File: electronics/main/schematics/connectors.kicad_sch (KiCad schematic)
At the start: 2 parts, among them J1 IN, J2 SW

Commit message: aux voltage
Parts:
- added X1, X3: 345V - Lila, TestPoint:TestPoint_THTPad_D3.0mm_Drill1.5mm, symbol Connector:TestPoint
- added X2: CT_HV - Grau, TestPoint:TestPoint_THTPad_D3.0mm_Drill1.5mm, symbol Connector:TestPoint
- added X4, X6: 3.13V - Grün, TestPoint:TestPoint_THTPad_D3.0mm_Drill1.5mm, symbol Connector:TestPoint
- added X5: CT_HEAT - Schwarz, TestPoint:TestPoint_THTPad_D3.0mm_Drill1.5mm, symbol Connector:TestPoint
- added X7: 12,6V - Rot, TestPoint:TestPoint_THTPad_D3.0mm_Drill1.5mm, symbol Connector:TestPoint
- added X8: 0V - Rot, TestPoint:TestPoint_THTPad_D3.0mm_Drill1.5mm, symbol Connector:TestPoint
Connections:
- new net V_Aux_N: X8.1
- new net V_Aux_P: X7.1
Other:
- note added: "Aux Voltage Input"
- note added: "Foot Switch Input"
- note added: "Guitar Input"
- note added: "HV Input"
- note added: "Heater Power Input"
- moved on the sheet: J1, J2

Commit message: widerstände angelegt
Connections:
- net GND-AUD: now reaches J1.1
- net GND-AUD: now also J1.4, J1.5, J1.6
- net Audio_IN: now reaches J1.2
- net Audio_IN: now also J1.3
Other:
- moved on the sheet: J1
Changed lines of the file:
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@@
+		)
+	)
+	(junction
+		(at 58.42 36.83)
+		(diameter 0)
+		(color 0 0 0 0)
+	)
+	(junction
+		(at 58.42 31.75)
+		(diameter 0)
+		(color 0 0 0 0)
+	)
+	(junction
+		(at 58.42 39.37)
+		(diameter 0)
+		(color 0 0 0 0)
+	)
+	(junction
+		(at 53.34 26.67)
+		(diameter 0)
+		(color 0 0 0 0)
+	)
+	(wire
+		(pts
+			(xy 49.53 29.21) (xy 58.42 29.21)
+		)
+		(stroke
+			(width 0)
+			(type default)
+		)
+	)
+	(wire
+		(pts
+			(xy 53.34 26.67) (xy 58.42 26.67)
+		)
+		(stroke
+			(width 0)
+			(type default)
 		)
 	)
@@
 	(wire
 		(pts
+			(xy 58.42 36.83) (xy 58.42 39.37)
+		)
+		(stroke
+			(width 0)
+			(type default)
+		)
+	)
+	(wire
+		(pts
+			(xy 58.42 29.21) (xy 58.42 31.75)
+		)
+		(stroke
+			(width 0)
+			(type default)
+		)
+	)
+	(wire
+		(pts
+			(xy 49.53 31.75) (xy 58.42 31.75)
+		)
+		(stroke
+			(width 0)
+			(type default)
+		)
+	)
+	(wire
+		(pts
+			(xy 58.42 39.37) (xy 58.42 41.91)
+		)
+		(stroke
+			(width 0)
+			(type default)
+		)
+	)
+	(wire
+		(pts
+			(xy 53.34 34.29) (xy 53.34 26.67)
+		)
+		(stroke
+			(width 0)
+			(type default)
+		)
+	)
+	(wire
+		(pts
+			(xy 49.53 34.29) (xy 53.34 34.29)
+		)
+		(stroke
+			(width 0)
+			(type default)
+		)
+	)
+	(wire
+		(pts
+			(xy 49.53 39.37) (xy 58.42 39.37)
+		)
+		(stroke
+			(width 0)
+			(type default)
+		)
+	)
+	(wire
+		(pts
+			(xy 58.42 31.75) (xy 58.42 36.83)
+		)
+		(stroke
+			(width 0)
+			(type default)
+		)
+	)
+	(wire
+		(pts
+			(xy 49.53 36.83) (xy 58.42 36.83)
+		)
+		(stroke
+			(width 0)
+			(type default)
+		)
+	)
+	(wire
+		(pts
 			(xy 40.64 175.26) (xy 54.61 175.26)
+		)
+		(stroke
+			(width 0)
+			(type default)
+		)
+	)
+	(wire
+		(pts
+			(xy 49.53 26.67) (xy 53.34 26.67)
 		)
 		(stroke
@@
 		)
 	)
+	(hierarchical_label "Audio_IN"
+		(shape output)
+		(at 58.42 26.67 0)
+		(effects
+			(font
+				(size 1.27 1.27)
+			)
+			(justify left)
+		)
+	)
 	(symbol
 		(lib_id "Connector:TestPoint")
@@
 	(symbol
 		(lib_id "wb50_symbols:WB50_Jack_TRS_6pin_Switched")
-		(at 41.91 35.56 0)
+		(at 41.91 33.02 0)
 		(unit 1)
 		(exclude_from_sim no)
@@
 		(fields_autoplaced yes)
 		(property "Reference" "J1"
+			(at 40.64 17.78 0)
+			(effects
+				(font
+					(size 1.27 1.27)
+				)
+			)
+		)
+		(property "Value" "IN"
 			(at 40.64 20.32 0)
 			(effects
@@
 			)
 		)
-		(property "Value" "IN"
+		(property "Footprint" "wb50_footprints:WB50_Jack_TRS_6pin_16.2mm"
 			(at 40.64 22.86 0)
 			(effects
@@
 			)
 		)
-		(property "Footprint" "wb50_footprints:WB50_Jack_TRS_6pin_16.2mm"
-			(at 40.64 25.4 0)
-			(effects
-				(font
-					(size 1.27 1.27)
-				)
-			)
-		)
 		(property "Datasheet" ""
-			(at 41.91 35.56 0)
+			(at 41.91 33.02 0)
 			(effects
 				(font
@@
 		)
 		(property "Description" ""
-			(at 41.91 35.56 0)
+			(at 41.91 33.02 0)
 			(effects
 				(font
@@
 					(unit 1)
 				)
+			)
+		)
+	)
+	(symbol
+		(lib_id "power:GND")
+		(at 58.42 41.91 0)
+		(unit 1)
+		(exclude_from_sim no)
+		(in_bom yes)
+		(on_board yes)
+		(dnp no)
+		(fields_autoplaced yes)
+		(property "Reference" "#PWR07"
+			(at 58.42 48.26 0)
+			(effects
+				(font
+					(size 1.27 1.27)
+				)
+				(hide yes)
+			)
+		)
+		(property "Value" "GND-AUD"
+			(at 58.42 46.99 0)
+			(effects
+				(font
+					(size 1.27 1.27)
+				)
+			)
+		)
+		(property "Footprint" ""
+			(at 58.42 41.91 0)
+			(effects
+				(font
+					(size 1.27 1.27)
+				)
+				(hide yes)
+			)
+		)
+		(property "Datasheet" ""
+			(at 58.42 41.91 0)
+			(effects
+				(font
+					(size 1.27 1.27)
+				)
+				(hide yes)
+			)
+		)
+		(property "Description" "Power symbol creates a global label with name \"GND\" , ground"
+			(at 58.42 41.91 0)
+			(effects
+				(font
+					(size 1.27 1.27)
+				)
+				(hide yes)
+			)
+		)
+		(pin "1"
+		)
+		(instances
+			(project ""
+				(path "/6805e3ef-87bd-473d-890f-05ae2da73c1a/71fb01be-e2af-43a2-ab1d-1ec35077c210"
+					(reference "#PWR07")
+					(unit 1)
+				)

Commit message: schematic ready? - check
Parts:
- removed X1, X3: 345V - Lila, TestPoint:TestPoint_THTPad_D3.0mm_Drill1.5mm, symbol Connector:TestPoint
- removed X2: CT_HV - Grau, TestPoint:TestPoint_THTPad_D3.0mm_Drill1.5mm, symbol Connector:TestPoint
- removed X4, X6: 3.13V - Grün, TestPoint:TestPoint_THTPad_D3.0mm_Drill1.5mm, symbol Connector:TestPoint
- removed X5: CT_HEAT - Schwarz, TestPoint:TestPoint_THTPad_D3.0mm_Drill1.5mm, symbol Connector:TestPoint
- removed X7: 12,6V - Rot, TestPoint:TestPoint_THTPad_D3.0mm_Drill1.5mm, symbol Connector:TestPoint
- removed X8: 0V - Rot, TestPoint:TestPoint_THTPad_D3.0mm_Drill1.5mm, symbol Connector:TestPoint
- added J3: OUT1, wb50_footprints:WB50_Jack_TRS_6pin_16.2mm, symbol wb50_symbols:WB50_Jack_TRS_6pin_Switched
- added J4: OUT2, wb50_footprints:WB50_Jack_TRS_6pin_16.2mm, symbol wb50_symbols:WB50_Jack_TRS_6pin_Switched
- added X12: GND_OT, TestPoint:TestPoint_THTPad_D4.0mm_Drill2.0mm, symbol Connector:TestPoint
- added X9: Audio IN, TestPoint:TestPoint_THTPad_D4.0mm_Drill2.0mm, symbol Connector:TestPoint
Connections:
- new net: J3.1, J4.1, J4.6, X12.1
- new net: J3.6, J4.4, J4.5
- new net NFB_IN: J3.2, J3.3, J3.4, J3.5, J4.2, J4.3, X9.1
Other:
- note added: "GND vom OT Sternpunkt"
- note added: "Kabel von Impedanzwahlschalter"
- note added: "Speaker Output"
- note removed: "Aux Voltage Input"
- note removed: "HV Input"
- note removed: "Heater Power Input"

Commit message: schematic  checked!
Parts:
- added X1: Switch-ON, TestPoint:TestPoint_THTPad_D2.0mm_Drill1.0mm, symbol Connector:TestPoint
- added X2: Switch-GND, TestPoint:TestPoint_THTPad_D2.0mm_Drill1.0mm, symbol Connector:TestPoint
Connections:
- net GND-AUD: now also J3.1 (S), J4.1 (S), J4.6 (SN), X12.1
- net GND-AUX: now reaches J2.1 (S)
- net GND-AUX: now also J2.6 (SN), X2.1
- net REL-SW: now reaches J2.2 (R)
- net REL-SW: now also J2.3 (T)
- net at J2.4 (TN): now also J2.5 (RN), X1.1

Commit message: updated PCB
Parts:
- X1, X2: footprint TestPoint:TestPoint_THTPad_D2.0mm_Drill1.0mm -> TestPoint:TestPoint_THTPad_D3.0mm_Drill1.5mm
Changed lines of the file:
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@@
 			)
 		)
-		(property "Footprint" "TestPoint:TestPoint_THTPad_D2.0mm_Drill1.0mm"
+		(property "Footprint" "TestPoint:TestPoint_THTPad_D3.0mm_Drill1.5mm"
 			(at 82.55 82.55 0)
 			(effects
@@
 			)
 		)
-		(property "Footprint" "TestPoint:TestPoint_THTPad_D2.0mm_Drill1.0mm"
+		(property "Footprint" "TestPoint:TestPoint_THTPad_D3.0mm_Drill1.5mm"
 			(at 82.55 74.93 0)
 			(effects

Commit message: update design
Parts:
- removed X1: Switch-ON, TestPoint:TestPoint_THTPad_D3.0mm_Drill1.5mm, symbol Connector:TestPoint
- removed X2: Switch-GND, TestPoint:TestPoint_THTPad_D3.0mm_Drill1.5mm, symbol Connector:TestPoint
- added U34: ST-0-102-C03-N003-RS, footprints:SW-TH_ST-0-102-C03-N003-RS, symbol symbols:ST-0-102-C03-N003-RS
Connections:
- net GND-AUX: now also U34.3
- net at J2.4 (TN), J2.5 (RN): now also U34.2
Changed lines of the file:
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@@
+	)
+	(junction
+		(at 82.55 69.85)
+		(diameter 0)
+		(color 0 0 0 0)
 	)
 	(junction
@@
 	)
 	(junction
-		(at 82.55 69.85)
-		(diameter 0)
-		(color 0 0 0 0)
-	)
-	(junction
 		(at 232.41 53.34)
 		(diameter 0)
@@
 	(wire
 		(pts
+			(xy 95.25 77.47) (xy 95.25 78.74)
+		)
+		(stroke
+			(width 0)
+			(type default)
+		)
+	)
+	(wire
+		(pts
 			(xy 260.35 76.2) (xy 254 76.2)
 		)
@@
 	(wire
 		(pts
+			(xy 110.49 76.2) (xy 115.57 76.2)
+		)
+		(stroke
+			(width 0)
+			(type default)
+		)
+	)
+	(wire
+		(pts
 			(xy 53.34 26.67) (xy 58.42 26.67)
 		)
@@
 	(wire
 		(pts
-			(xy 57.15 77.47) (xy 82.55 77.47)
+			(xy 57.15 77.47) (xy 95.25 77.47)
 		)
 		(stroke
@@
 	(wire
 		(pts
+			(xy 115.57 69.85) (xy 82.55 69.85)
+		)
+		(stroke
+			(width 0)
+			(type default)
+		)
+	)
+	(wire
+		(pts
 			(xy 247.65 25.4) (xy 260.35 25.4)
 		)
@@
 	(wire
 		(pts
+			(xy 95.25 78.74) (xy 100.33 78.74)
+		)
+		(stroke
+			(width 0)
+			(type default)
+		)
+	)
+	(wire
+		(pts
 			(xy 49.53 34.29) (xy 53.34 34.29)
 		)
@@
 		(pts
 			(xy 254 76.2) (xy 212.09 76.2)
+		)
+		(stroke
+			(width 0)
+			(type default)
+		)
+	)
+	(wire
+		(pts
+			(xy 115.57 76.2) (xy 115.57 69.85)
 		)
 		(stroke
@@
 			)
 			(justify right)
+		)
+	)
+	(symbol
+		(lib_id "symbols:ST-0-102-C03-N003-RS")
+		(at 105.41 76.2 0)
+		(mirror y)
+		(unit 1)
+		(exclude_from_sim no)
+		(in_bom yes)
+		(on_board yes)
+		(dnp no)
+		(property "Reference" "U34"
+			(at 105.41 68.58 0)
+			(effects
+				(font
+					(size 1.27 1.27)
+				)
+			)
+		)
+		(property "Value" "ST-0-102-C03-N003-RS"
+			(at 105.41 71.12 0)
+			(effects
+				(font
+					(size 1.27 1.27)
+				)
+			)
+		)
+		(property "Footprint" "footprints:SW-TH_ST-0-102-C03-N003-RS"
+			(at 105.41 86.36 0)
+			(effects
+				(font
+					(size 1.27 1.27)
+					(italic yes)
+				)
+				(hide yes)
+			)
+		)
+		(property "Datasheet" "https://item.szlcsc.com/1879280.html"
+			(at 107.696 76.073 0)
+			(effects
+				(font
+					(size 1.27 1.27)
+				)
+				(justify left)
+				(hide yes)
+			)
+		)
+		(property "Description" ""
+			(at 105.41 76.2 0)
+			(effects
+				(font
+					(size 1.27 1.27)
+				)
+				(hide yes)
+			)
+		)
+		(property "LCSC" "C1788489"
+			(at 105.41 76.2 0)
+			(effects
+				(font
+					(size 1.27 1.27)
+				)
+				(hide yes)
+			)
+		)
+		(pin "1"
+		)
+		(pin "2"
+		)
+		(pin "5"
+		)
+		(pin "4"
+		)
+		(pin "3"
+		)
+		(instances
+			(project ""
+				(path "/6805e3ef-87bd-473d-890f-05ae2da73c1a/71fb01be-e2af-43a2-ab1d-1ec35077c210"
+					(reference "U34")
+					(unit 1)
+				)
+			)
 		)
 	)
@@
 	)
 	(symbol
-		(lib_id "Connector:TestPoint")
-		(at 82.55 77.47 270)
-		(unit 1)
-		(exclude_from_sim no)
-		(in_bom yes)
-		(on_board yes)
-		(dnp no)
-		(property "Reference" "X2"
-			(at 88.9 82.042 90)
-			(effects
-				(font
-					(size 1.27 1.27)
-				)
-				(justify left)
-			)
-		)
-		(property "Value" "Switch-GND"
-			(at 88.646 79.756 90)
-			(effects
-				(font
-					(size 1.27 1.27)
-				)
-				(justify left)
-			)
-		)
-		(property "Footprint" "TestPoint:TestPoint_THTPad_D3.0mm_Drill1.5mm"
-			(at 82.55 82.55 0)
-			(effects
-				(font
-					(size 1.27 1.27)
-				)
-				(hide yes)
-			)
-		)
-		(property "Datasheet" "~"
-			(at 82.55 82.55 0)
-			(effects
-				(font
-					(size 1.27 1.27)
-				)
-				(hide yes)
-			)
-		)
-		(property "Description" "test point"
-			(at 82.55 77.47 0)
-			(effects
-				(font
-					(size 1.27 1.27)
-				)
-				(hide yes)
-			)
-		)
-		(pin "1"
-		)
-		(instances
-			(project "wb50"
-				(path "/6805e3ef-87bd-473d-890f-05ae2da73c1a/71fb01be-e2af-43a2-ab1d-1ec35077c210"
-					(reference "X2")
-					(unit 1)
-				)
-			)
-		)
-	)
-	(symbol
 		(lib_id "wb50_symbols:WB50_Jack_TRS_6pin_Switched")
 		(at 41.91 33.02 0)
@@
 					(unit 1)
 				)
-			)
-		)
-	)
-	(symbol
-		(lib_id "Connector:TestPoint")
-		(at 82.55 69.85 270)
-		(unit 1)
-		(exclude_from_sim no)
-		(in_bom yes)
-		(on_board yes)
-		(dnp no)
-		(property "Reference" "X1"
-			(at 88.9 74.422 90)
-			(effects
-				(font
-					(size 1.27 1.27)
-				)
-				(justify left)
-			)
-		)
-		(property "Value" "Switch-ON"
-			(at 88.646 72.136 90)
-			(effects
-				(font
-					(size 1.27 1.27)
-				)
-				(justify left)
-			)
-		)
-		(property "Footprint" "TestPoint:TestPoint_THTPad_D3.0mm_Drill1.5mm"
-			(at 82.55 74.93 0)
-			(effects
-				(font
-					(size 1.27 1.27)
-				)
-				(hide yes)
-			)
-		)
-		(property "Datasheet" "~"
-			(at 82.55 74.93 0)
-			(effects
-				(font
-					(size 1.27 1.27)
-				)
-				(hide yes)
-			)
-		)
-		(property "Description" "test point"
-			(at 82.55 69.85 0)
-			(effects
-				(font
-					(size 1.27 1.27)
-				)
-				(hide yes)
-			)
-		)
-		(pin "1"
-		)
-		(instances
-			(project "wb50"
-				(path "/6805e3ef-87bd-473d-890f-05ae2da73c1a/71fb01be-e2af-43a2-ab1d-1ec35077c210"
-					(reference "X1")
-					(unit 1)
-				)

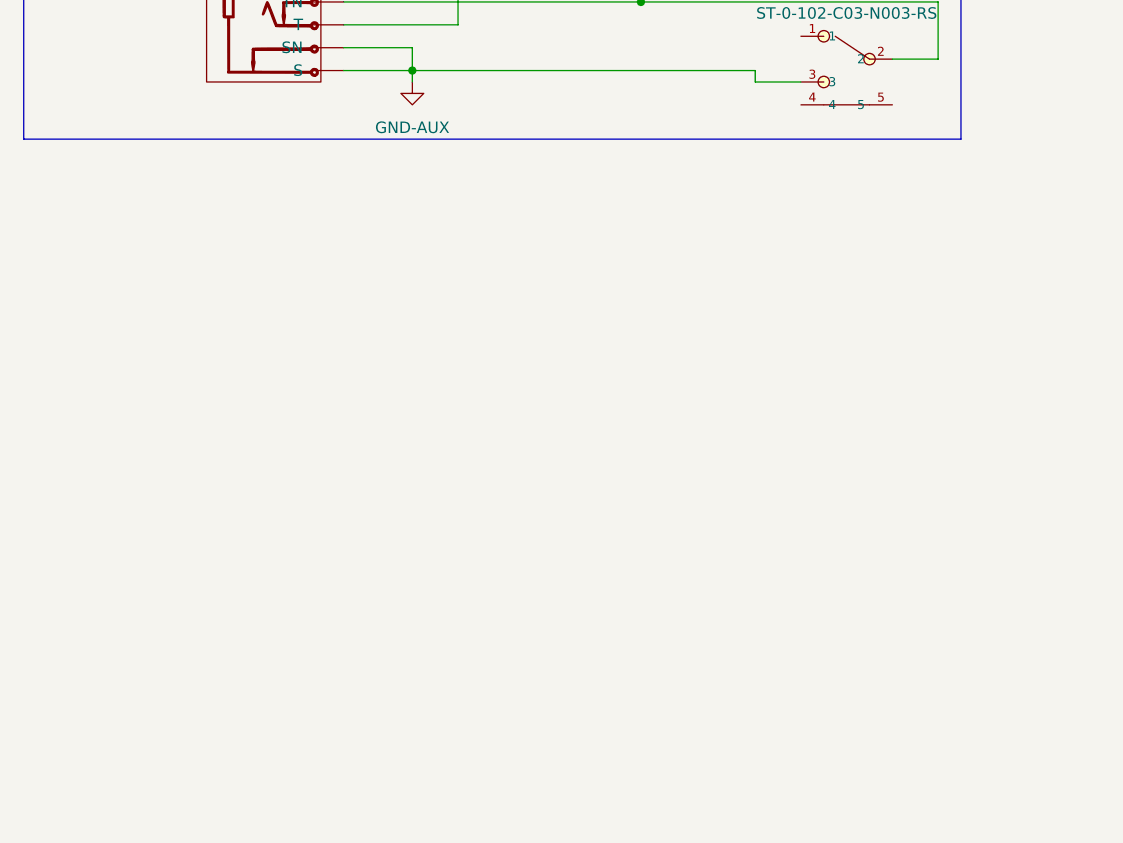
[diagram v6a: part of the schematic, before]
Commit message: add fx loop, add new shield
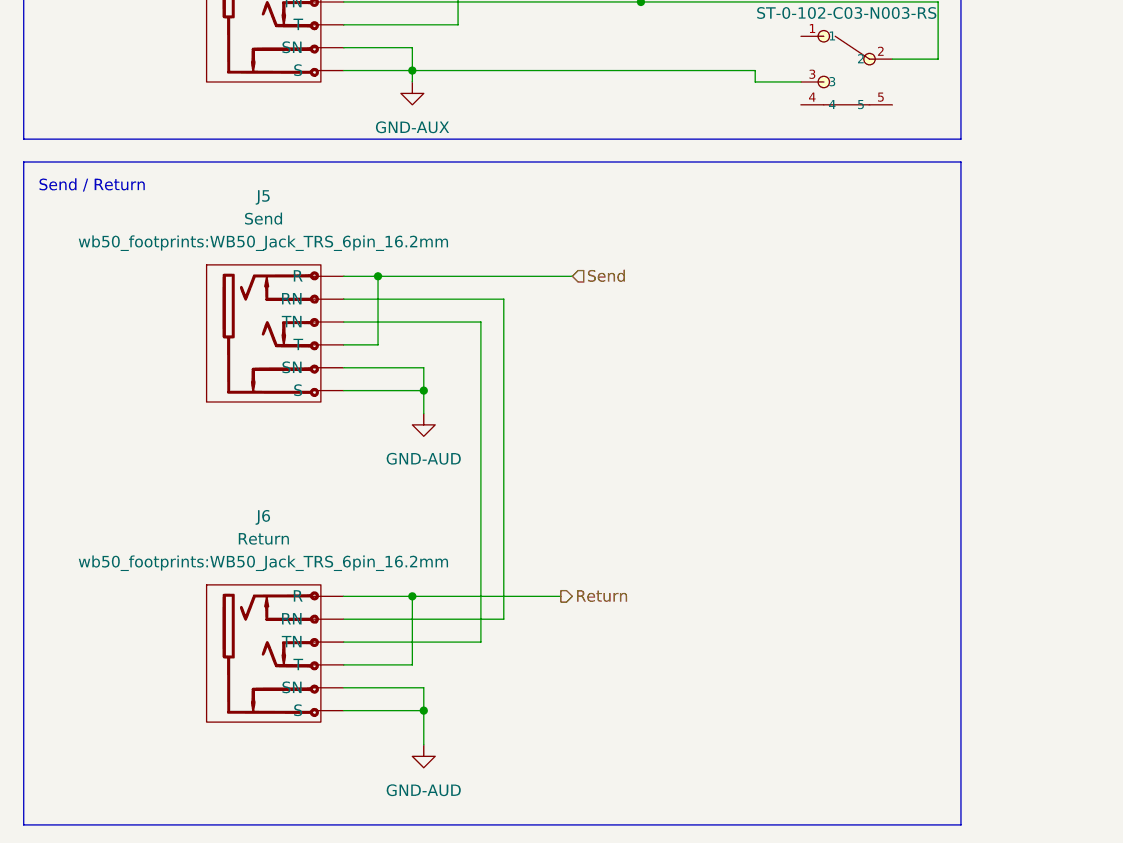
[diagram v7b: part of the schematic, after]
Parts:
- added J5: Send, wb50_footprints:WB50_Jack_TRS_6pin_16.2mm, symbol wb50_symbols:WB50_Jack_TRS_6pin_Switched
- added J6: Return, wb50_footprints:WB50_Jack_TRS_6pin_16.2mm, symbol wb50_symbols:WB50_Jack_TRS_6pin_Switched
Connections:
- net GND-AUD: now also J5.1 (S), J5.6 (SN), J6.1 (S), J6.6 (SN)
- new net: J5.4 (TN), J6.4 (TN)
- new net: J5.5 (RN), J6.5 (RN)
- new net Return: J6.2 (R), J6.3 (T)
- new net Send: J5.2 (R), J5.3 (T)
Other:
- note added: "Send / Return"
